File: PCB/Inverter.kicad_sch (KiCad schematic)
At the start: 76 parts, among them J1 Conn_01x02_Pin, J2 Conn_01x03_Pin, J3 Conn_01x05_Pin, J4 Conn_01x04_Pin, Q1 STP60NF06, Q2 STP60NF06, Q3 STP60NF06, Q4 STP60NF06, Q5 STP60NF06, Q6 STP60NF06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

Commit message: Change#000
Start second try
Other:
- company: (none) -> By #Tech01
- title: Inverter BLDC -> Simple BLDC motor controller
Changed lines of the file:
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@@
 	(paper "A4")
 	(title_block
-		(title "Inverter BLDC")
+		(title "Simple BLDC motor controller")
 		(date "2025-04-04")
 		(rev "V0.1")
+		(company "By #Tech01")
 	)
 	(text_box "Connectors"

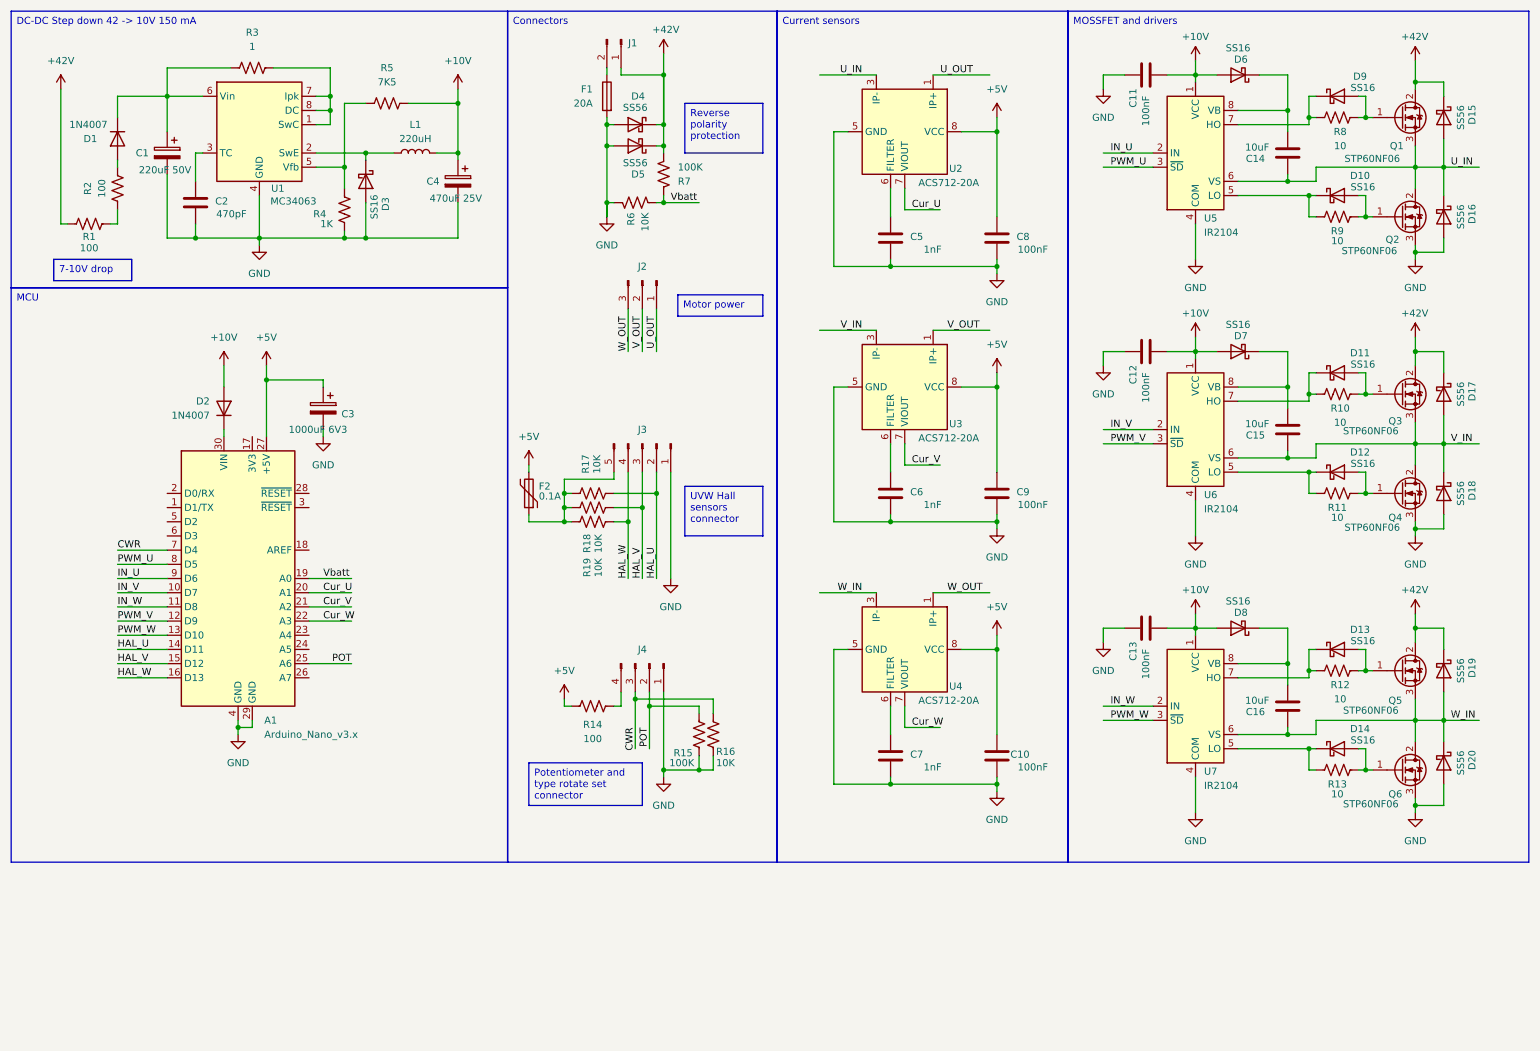
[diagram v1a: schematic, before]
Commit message: Change#001
I replaced the DC-DC converter chip with a higher voltage one, 80 V versus 40 V as before.
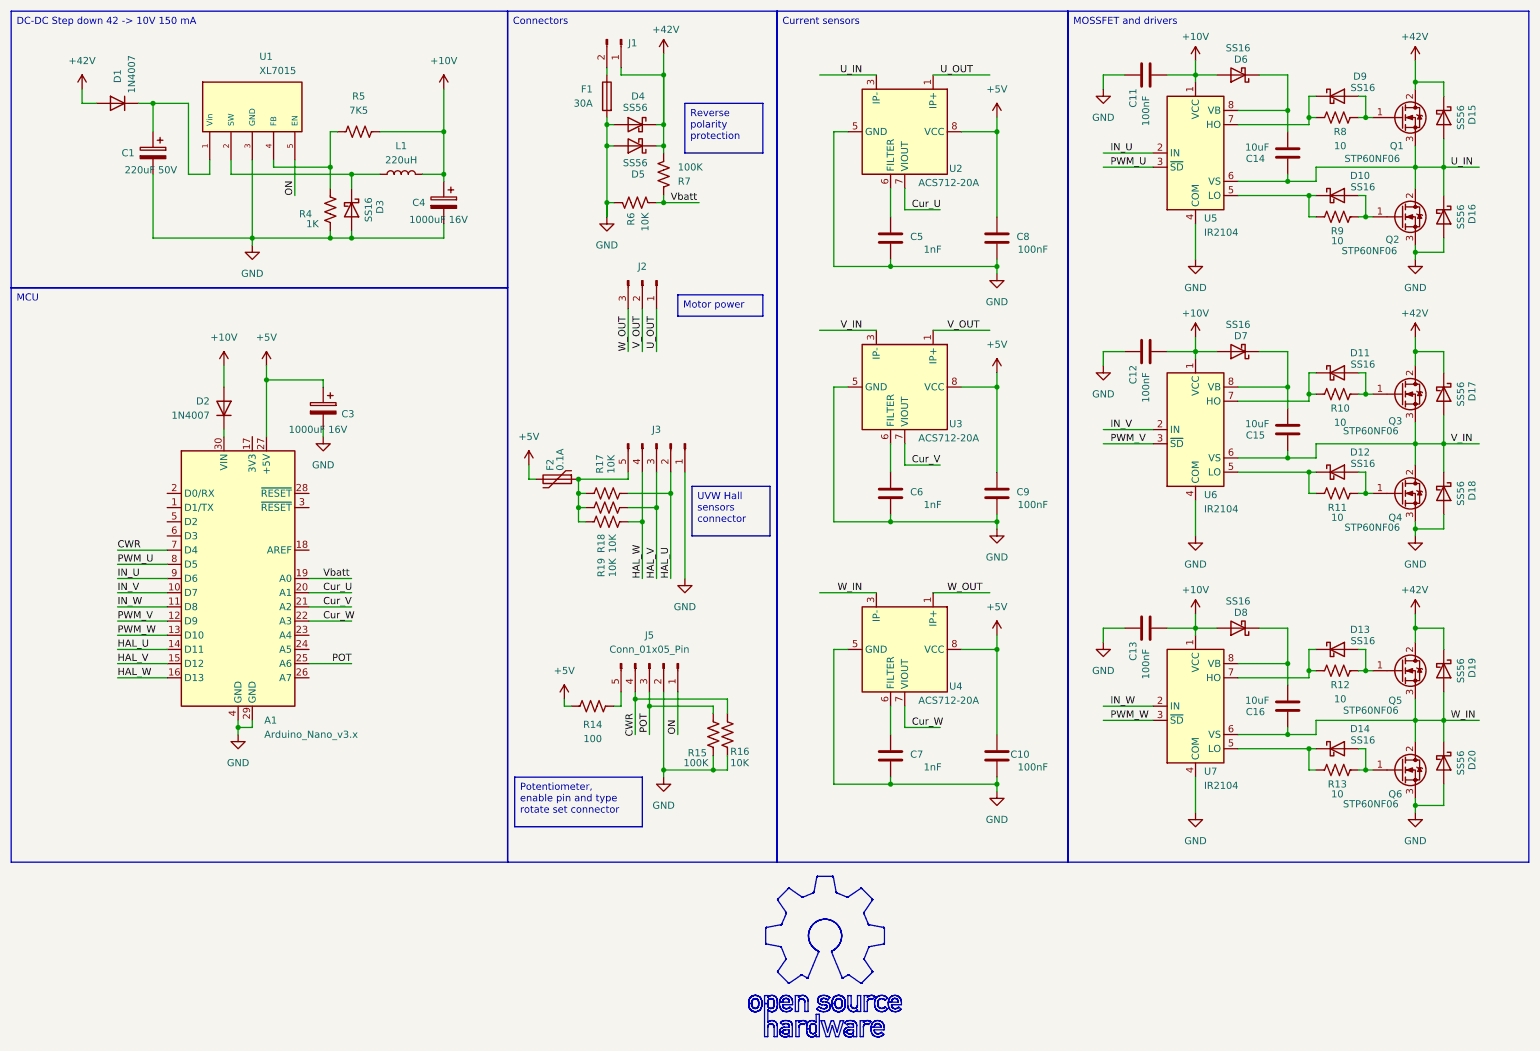
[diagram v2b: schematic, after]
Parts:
- removed C2: 470pF, Capacitor_SMD:C_0603_1608Metric_Pad1.08x0.95mm_HandSolder, symbol Device:C
- removed J4: Conn_01x04_Pin, Connector_Hirose:Hirose_DF13-04P-1.25DSA_1x04_P1.25mm_Vertical, symbol Connector:Conn_01x04_Pin
- removed R1, R2: 100, Resistor_SMD:R_1206_3216Metric_Pad1.30x1.75mm_HandSolder, symbol Device:R_US
- removed R3: 1, Resistor_SMD:R_0805_2012Metric_Pad1.20x1.40mm_HandSolder, symbol Device:R_US
- removed U1: MC34063, Package_SO:SOIC-8_3.9x4.9mm_P1.27mm, symbol Regulator_Switching:MC34063AD
- added J5: Conn_01x05_Pin, Connector_Hirose:Hirose_DF13-05P-1.25DSA_1x05_P1.25mm_Vertical, symbol Connector:Conn_01x05_Pin
- added U1: XL7015, Package_TO_SOT_SMD:TO-252-5_TabPin3, symbol XL7015:XL7015
- C3: value 1000uF 6V3 -> 1000uF 16V
- C4: value 470uF 25V -> 1000uF 16V
- F1: value 20A -> 30A; footprint Fuse:Fuseholder_Clip-5x20mm_Eaton_1A5601-01_Inline_P20.80x6.76mm_D1.70mm_Horizontal -> Fuse:FUSE_3522-2
- Q1, Q2, Q3, Q4, Q5, Q6: footprint Package_TO_SOT_THT:TO-220-3_Vertical -> Package_TO_SOT_THT:TO-220-3_Horizontal_TabDown
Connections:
- net +42V: now also D1.2 (A)
- net CWR: now also J5.4 (Pin_4)
- net GND: now also J5.2 (Pin_2), U1.3 (GND)
- net POT: now also J5.3 (Pin_3)
- net at R4.2, R5.2: now also U1.4 (FB)
- net at R14.2: now also J5.5 (Pin_5)
- net at D3.1 (K), L1.1: now also U1.2 (SW)
- net at C1.1, D1.1 (K): now also U1.1 (Vin)
- new net ON: J5.1 (Pin_1), U1.5 (EN)
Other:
- moved on the sheet: C1, C4, D1, D3, F2, J3, L1, R15, R16, R17, R18, R19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

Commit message: #Change002
Add device parameters
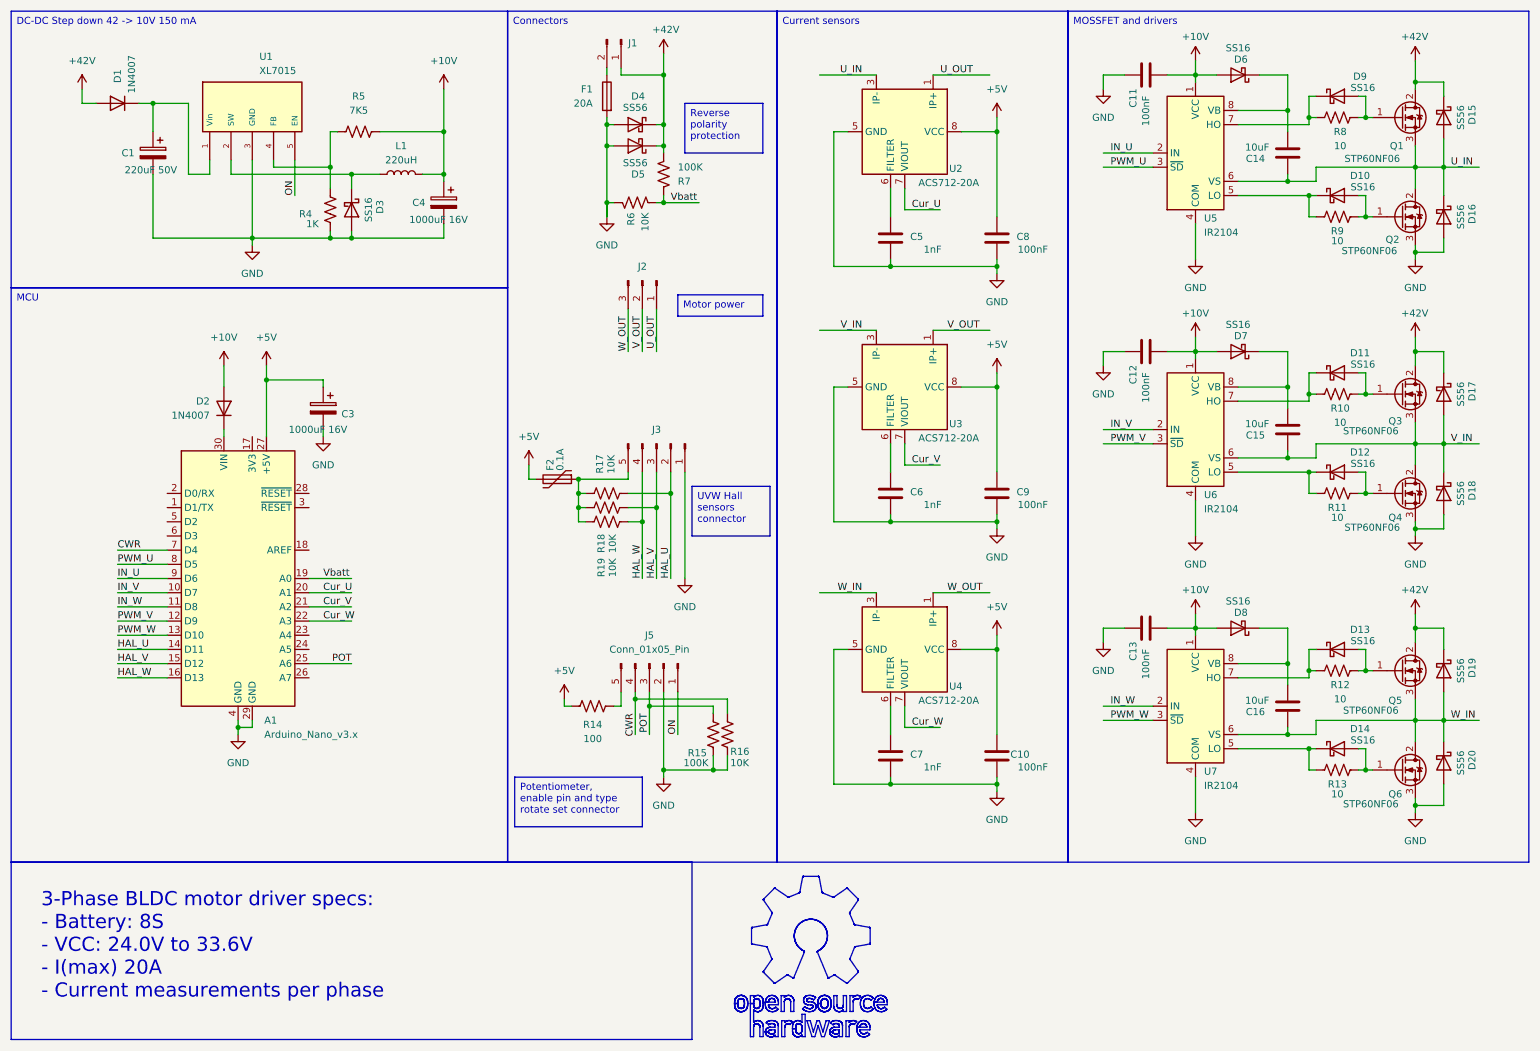
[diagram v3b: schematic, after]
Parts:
- F1: value 30A -> 20A
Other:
- company: By #Tech01 -> By Techn0man1ac

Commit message: Change#003
Schematic changes
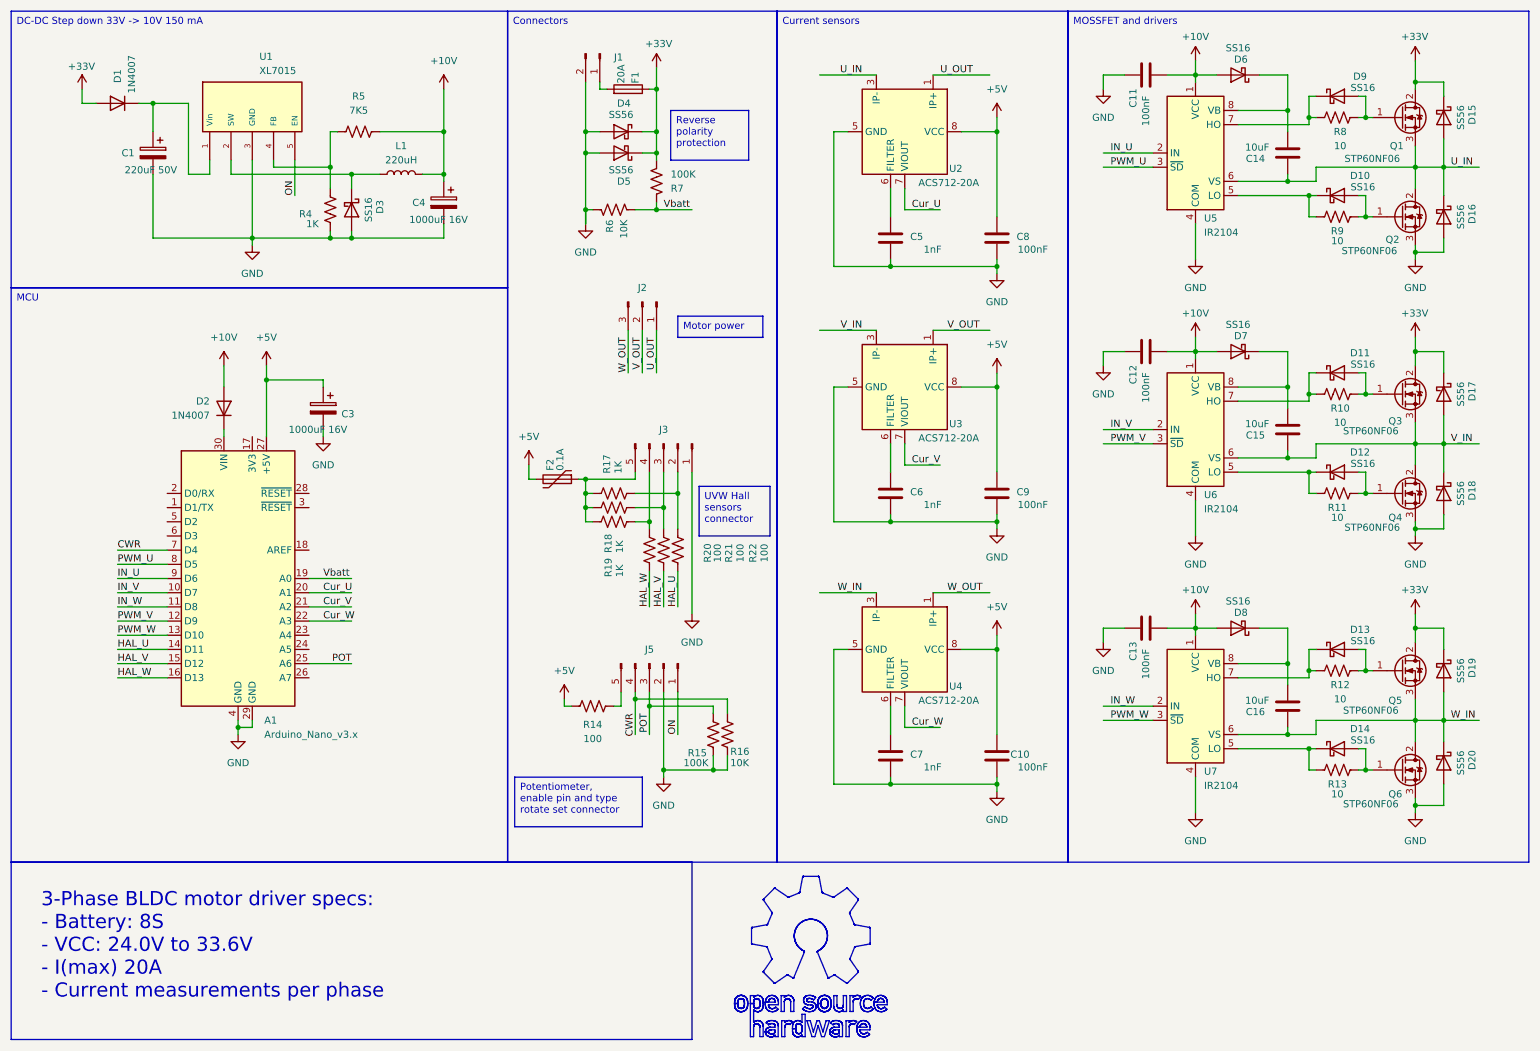
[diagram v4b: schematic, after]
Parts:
- added R20, R21, R22: 100, Resistor_SMD:R_1206_3216Metric_Pad1.30x1.75mm_HandSolder, symbol Device:R_US
- C14, C15, C16: footprint Capacitor_SMD:C_0603_1608Metric_Pad1.08x0.95mm_HandSolder -> Capacitor_SMD:C_0805_2012Metric_Pad1.18x1.45mm_HandSolder
- Q1, Q2, Q3, Q4, Q5, Q6: footprint Package_TO_SOT_THT:TO-220-3_Horizontal_TabDown -> Package_TO_SOT_THT:TO-220-3_Horizontal_TabUp
- R17, R18, R19: value 10K -> 1K
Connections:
- net GND: now also J1.2 (Pin_2); no longer F1.2
- net HAL_U: now also R22.1; no longer J3.2 (Pin_2), R17.1
- net HAL_V: now also R21.1; no longer J3.3 (Pin_3), R18.1
- net HAL_W: now also R20.1; no longer J3.4 (Pin_4), R19.1
- net +33V: now reaches F1.1
- net +33V: now also D1.2 (A), D15.1 (K), D17.1 (K), D19.1 (K), D4.1 (K), D5.1 (K), Q1.2 (D), Q3.2 (D), Q5.2 (D), R7.1; no longer J1.2 (Pin_2)
- removed net +42V: D1.2 (A), D15.1 (K), D17.1 (K), D19.1 (K), D4.1 (K), D5.1 (K), J1.1 (Pin_1), Q1.2 (D), Q3.2 (D), Q5.2 (D), R7.1
- new net: J3.3 (Pin_3), R18.1, R21.2
- new net: F1.2, J1.1 (Pin_1)
- new net: J3.4 (Pin_4), R19.1, R20.2
- new net: J3.2 (Pin_2), R17.1, R22.2
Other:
- moved on the sheet: D4, D5, F1, J1, J2, J3, R17, R18, R19, R6, R7
